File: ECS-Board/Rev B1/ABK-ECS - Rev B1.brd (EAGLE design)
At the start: 100 x 80 mm, 271 parts, among them J1 USB-B-S-RA, J10 FTSH-105-01-L-DV-NOPASTE, J11 22-05-7028-02, J12 RB1-125BAG1A, J2 MSTBA2, J3 22-05-7068-06, J4 22-05-7028-02, J5 22-05-7068-06, J6 22-05-7068-06, J7 22-05-7068-06, J8 22-05-7028-02, J9 FTSH-103-01-L-DV-NOPASTE, K1 G6K-2G-Y, SW1 B3FS-1015, SW2 B3FS-1015, T1 MMBT2907ALT3, T10 MMBT2222AL, T11 IRLML5103TRPBF, T12 MMBT2222AL, T13 IRLML5103TRPBF, T14 IRLML5103TRPBF, T15 IRLML5103TRPBF, T16 IRLML5103TRPBF, T17 MMBT2222AL, T18 MMBT2222AL, T19 MMBT2222AL, T2 EXMACHINA-LOGO-NAME, T20 MMBT2222AL, T3 IRLML5103TRPBF, T4 IRLML5103TRPBF, T5 IRLML5103TRPBF, T6 IRLML5103TRPBF, T7 MMBT2222AL, T8 MMBT2222AL, T9 MMBT2222AL, U1 AT24C512C-SSHM-B, U2 LPC1768FBD100, U3 LT3686HDDPBF, U4 LT3686HDDPBF, U5 CD4050BD, U6 CD4050BD, U7 DP83848JSQ/NOPB, X1 FC-135, X2 ASE-12, X3 3000, X4 ASE_50

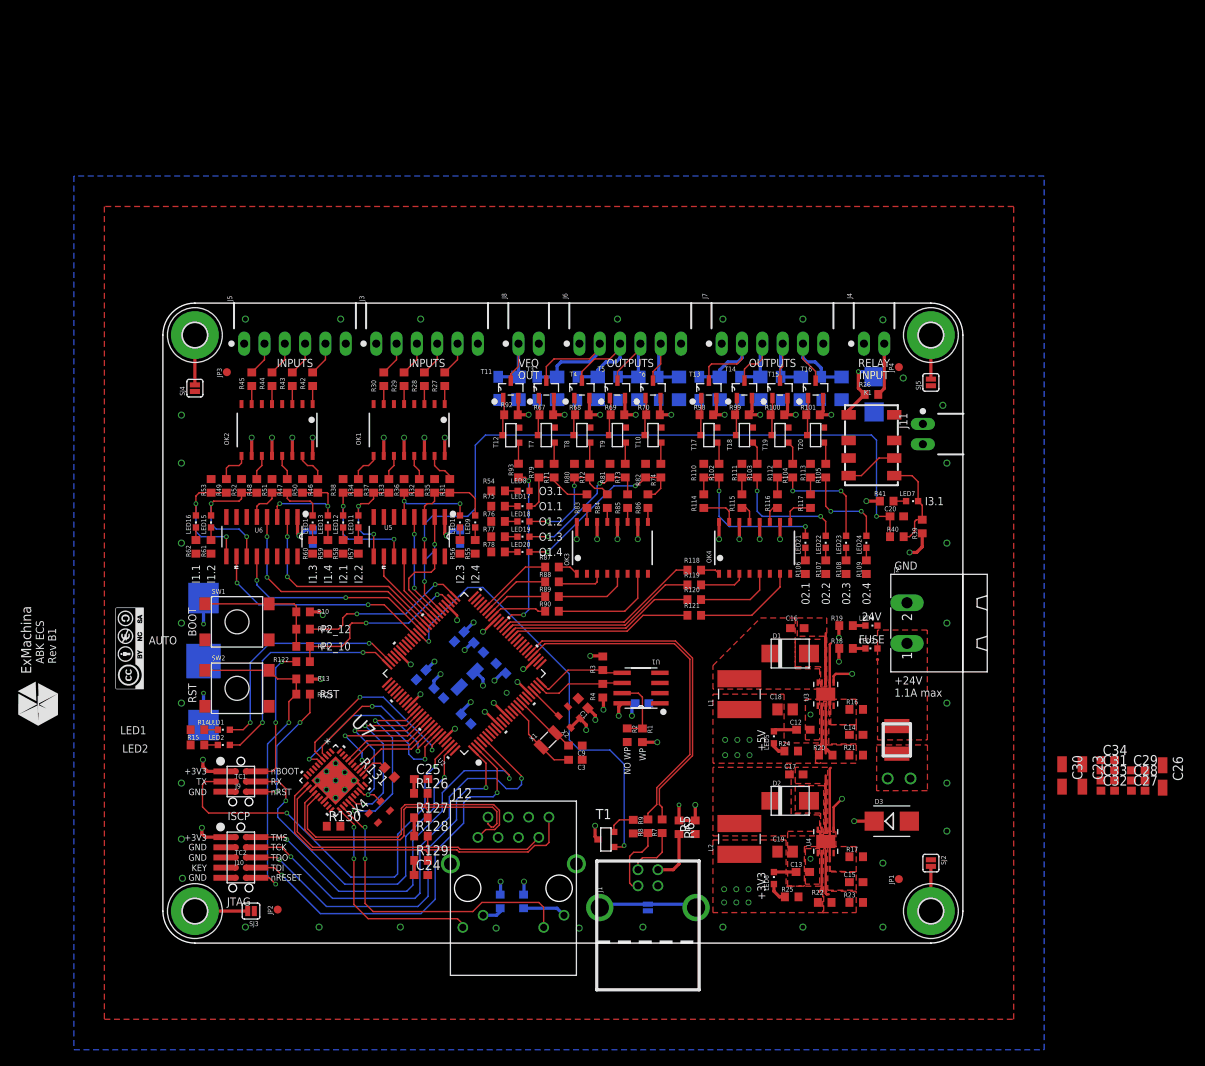
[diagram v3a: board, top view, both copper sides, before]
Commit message: Finish to route the board
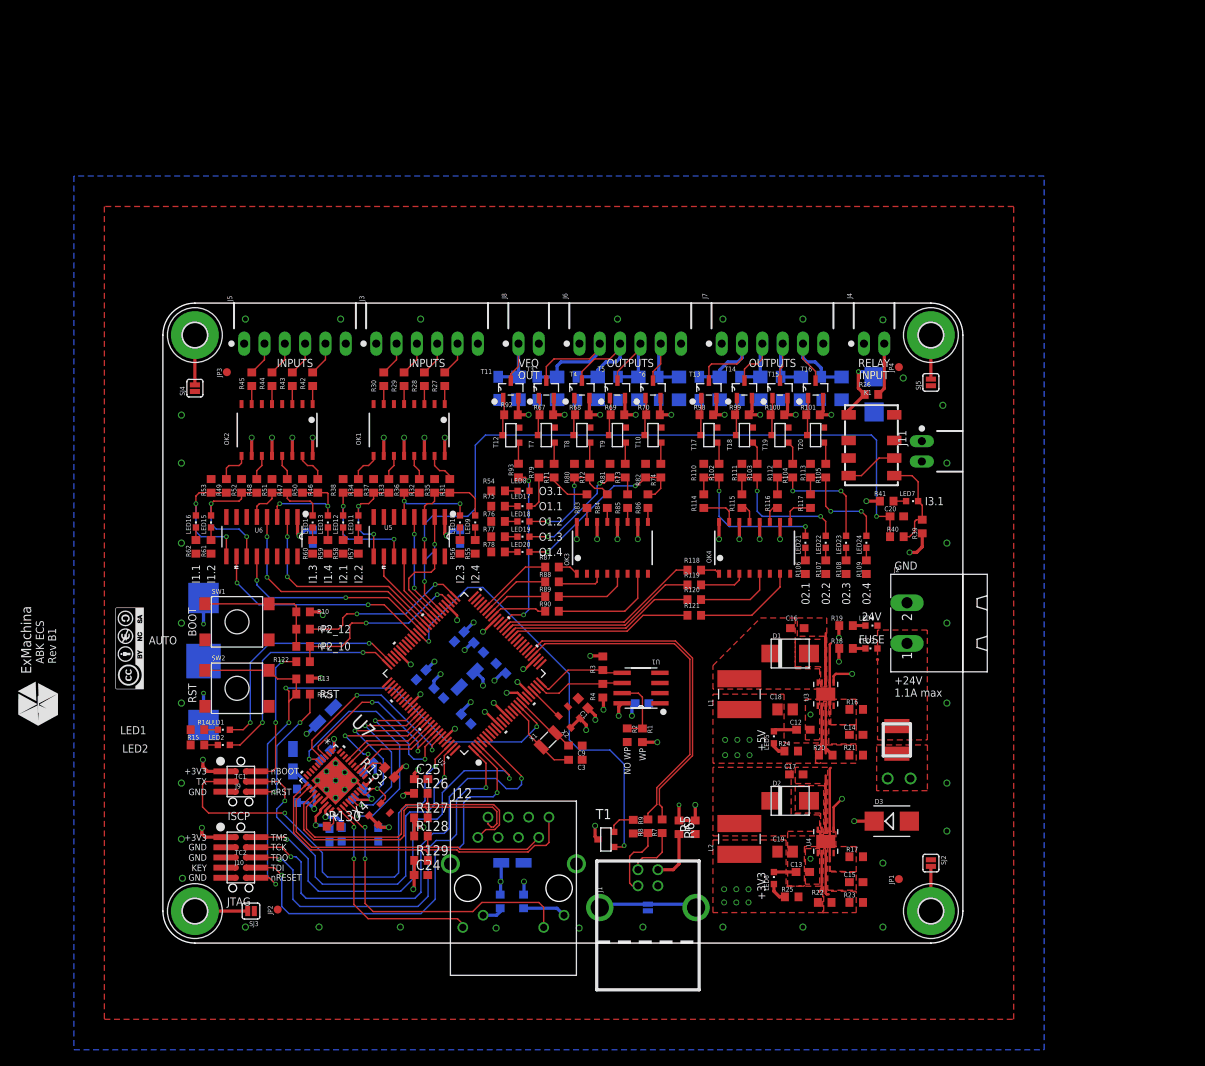
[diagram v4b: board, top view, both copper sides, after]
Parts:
- moved C26 108.7 mm to (16.3, 22.9), flipped to the bottom, turned to 90 degrees
- moved C28 105.2 mm to (16.8, 18.4), flipped to the bottom, turned to 90 degrees
- moved C27 99.7 mm to (22.4, 13.6), flipped to the bottom, turned to 270 degrees
- moved C33 97.8 mm to (20.3, 23.5), flipped to the bottom, turned to 315 degrees
- moved C32 97.4 mm to (20.8, 13.5), flipped to the bottom, turned to 270 degrees
- moved C29 96.3 mm to (25.7, 22.0), flipped to the bottom, turned to 315 degrees
- moved C31 93.8 mm to (24.4, 18.7), flipped to the bottom, turned to 315 degrees
- moved C30 92.4 mm to (20.3, 28.4), flipped to the bottom, turned to 135 degrees
- moved C34 91.7 mm to (26.9, 13.6), flipped to the bottom, turned to 270 degrees
- moved C23 72.1 mm to (43.7, 10.0), flipped to the bottom, turned to 180 degrees
- moved J11 2.16 mm to (94.9, 61.5)
- moved X4 0.25 mm to (27.1, 16.1)
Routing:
- net !RESET: track 43.5 -> 83.9 mm, vias 2 -> 4
- net PFBOUT: track 0.00 -> 28.7 mm, vias 0 -> 3
- net +3V3: track 83.1 -> 111.1 mm, vias 37 -> 47
- net AGND: track 0.00 -> 15.8 mm
- net JTAG_TDI: track 51.7 -> 55.5 mm
- net JTAG_TDO: track 49.0 -> 52.2 mm
- net JTAG_TCK: track 56.5 -> 59.7 mm
- net VBAT+: track 62.2 -> 59.1 mm
- net ISP_RXDO: track 47.7 -> 50.6 mm
- net N$116: track 0.00 -> 2.77 mm
- net JTAG_TMS: track 53.0 -> 55.6 mm
- net ISP_TXDO: track 54.1 -> 56.7 mm
- net ETH_X1: track 21.6 -> 23.7 mm
- net ETH_MDIO: track 22.7 -> 24.2 mm
- net ETH_TXD_EN: track 21.9 -> 23.1 mm
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
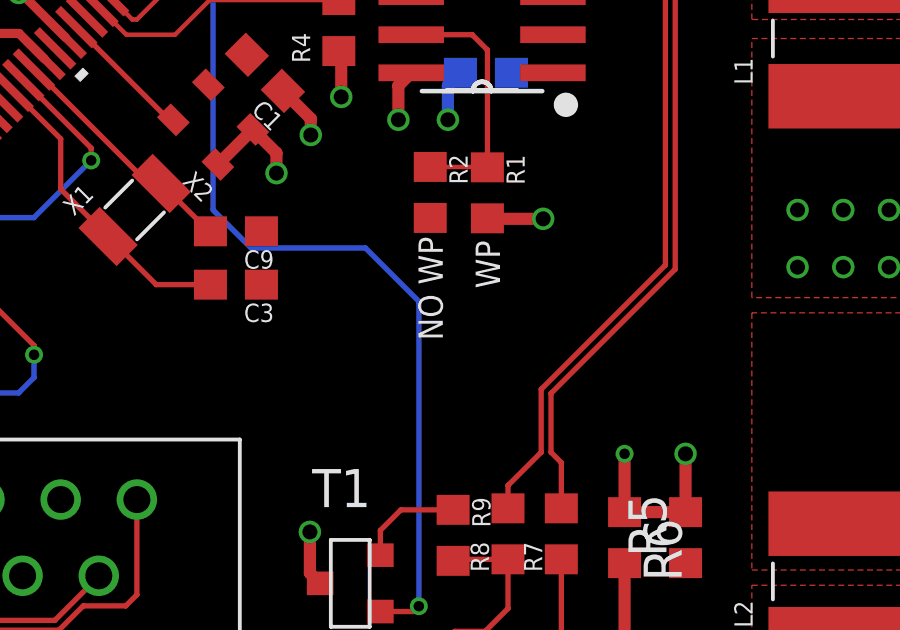
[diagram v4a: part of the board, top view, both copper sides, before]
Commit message: Add 0R to the USB Pull-up
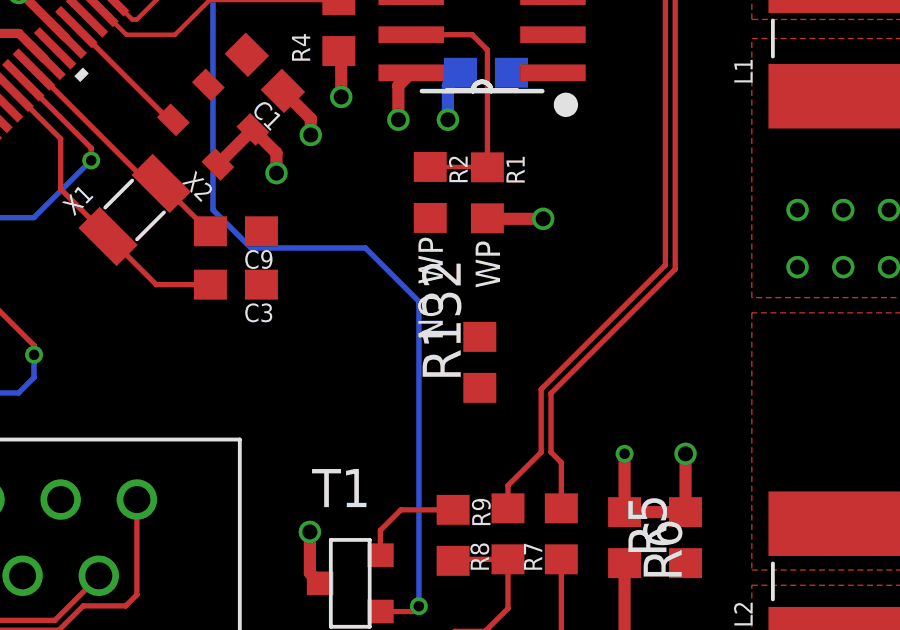
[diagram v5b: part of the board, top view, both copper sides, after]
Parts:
- added R132: 0R, rcl:R0603
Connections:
- net +3V3: now also R132.1
- net N$30: now also R132.2
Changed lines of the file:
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@@
 <layer number="14" name="Route14" color="1" fill="6" visible="no" active="no"/>
 <layer number="15" name="Route15" color="19" fill="1" visible="no" active="yes"/>
-<layer number="16" name="Bottom" color="21" fill="1" visible="no" active="yes"/>
+<layer number="16" name="Bottom" color="21" fill="1" visible="yes" active="yes"/>
 <layer number="17" name="Pads" color="18" fill="1" visible="yes" active="yes"/>
 <layer number="18" name="Vias" color="38" fill="1" visible="yes" active="yes"/>
@@
 <layer number="20" name="Dimension" color="7" fill="1" visible="yes" active="yes"/>
 <layer number="21" name="tPlace" color="55" fill="1" visible="yes" active="yes"/>
-<layer number="22" name="bPlace" color="54" fill="1" visible="no" active="yes"/>
+<layer number="22" name="bPlace" color="54" fill="1" visible="yes" active="yes"/>
 <layer number="23" name="tOrigins" color="15" fill="1" visible="yes" active="yes"/>
-<layer number="24" name="bOrigins" color="15" fill="1" visible="no" active="yes"/>
+<layer number="24" name="bOrigins" color="15" fill="1" visible="yes" active="yes"/>
 <layer number="25" name="tNames" color="55" fill="1" visible="no" active="yes"/>
-<layer number="26" name="bNames" color="54" fill="1" visible="no" active="yes"/>
+<layer number="26" name="bNames" color="54" fill="1" visible="yes" active="yes"/>
 <layer number="27" name="tValues" color="53" fill="1" visible="no" active="yes"/>
-<layer number="28" name="bValues" color="52" fill="1" visible="no" active="yes"/>
+<layer number="28" name="bValues" color="52" fill="1" visible="yes" active="yes"/>
 <layer number="29" name="tStop" color="7" fill="3" visible="no" active="yes"/>
 <layer number="30" name="bStop" color="7" fill="6" visible="no" active="yes"/>
@@
 <layer number="50" name="dxf" color="7" fill="1" visible="no" active="yes"/>
 <layer number="51" name="tDocu" color="55" fill="1" visible="yes" active="yes"/>
-<layer number="52" name="bDocu" color="54" fill="1" visible="no" active="yes"/>
+<layer number="52" name="bDocu" color="54" fill="1" visible="yes" active="yes"/>
 <layer number="53" name="tGND_GNDA" color="7" fill="1" visible="no" active="yes"/>
 <layer number="54" name="bGND_GNDA" color="7" fill="1" visible="no" active="yes"/>
@@
 <attribute name="OC_NEWARK" value="25M1728" x="284.099" y="1.778" size="1.778" layer="27" rot="R90" display="off"/>
 </element>
+<element name="R132" library="rcl" package="R0603" value="0R" x="59.69" y="20.32" rot="R90">
+<attribute name="MPN" value="RC0603FR-070RL" x="59.69" y="20.32" size="1.778" layer="27" rot="R90" display="off"/>
+<attribute name="OC_NEWARK" value="50Y7761" x="59.69" y="20.32" size="1.778" layer="27" rot="R90" display="off"/>
+<attribute name="MF" value="" x="59.69" y="20.32" size="1.778" layer="27" rot="R90" display="off"/>
+</element>
 </elements>
 <signals>
@@
 <wire x1="31.408003125" y1="8.511965625" x2="31.408003125" y2="6.8375625" width="0.4064" layer="1"/>
 <wire x1="31.408003125" y1="6.8375625" x2="31.29985" y2="6.729409375" width="0.4064" layer="1"/>
+<contactref element="R132" pad="1"/>
+<wire x1="54.026" y1="14.6685" x2="59.69" y2="19.47" width="0" layer="19" extent="1-1"/>
 </signal>
 <signal name="JTAG_TDO" class="1">
@@
 <wire x1="56.3753" y1="14.7193" x2="57.06" y2="15.404" width="0.1778" layer="1"/>
 <wire x1="57.06" y1="15.404" x2="58.801" y2="15.404" width="0.1778" layer="1"/>
+<contactref element="R132" pad="2"/>
+<wire x1="58.801" y1="15.404" x2="59.69" y2="21.17" width="0" layer="19" extent="1-1"/>
 </signal>
 <signal name="USB_CONNECT">

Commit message: Routing improvement
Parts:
- R132: value 0R -> 0R, DNI
- moved T2 40.3 mm to (16.1, 5.03), turned to 0 degrees
- moved CC1 38.0 mm to (23.6, 10.9), turned to 0 degrees
- moved R132 5.59 mm to (55.4, 16.8), turned to 0 degrees
- moved C26 0.13 mm to (16.4, 22.9)
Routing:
- net N$30: track 3.53 -> 7.10 mm
- net +3V3: track 111.1 -> 113.0 mm, vias 47 -> 48
- net ISP_RXDO: track 50.6 -> 51.2 mm
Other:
- board text added: "ISP_BOOT"
- board text added: "ISP_RST"
- board text removed: "AUTO"

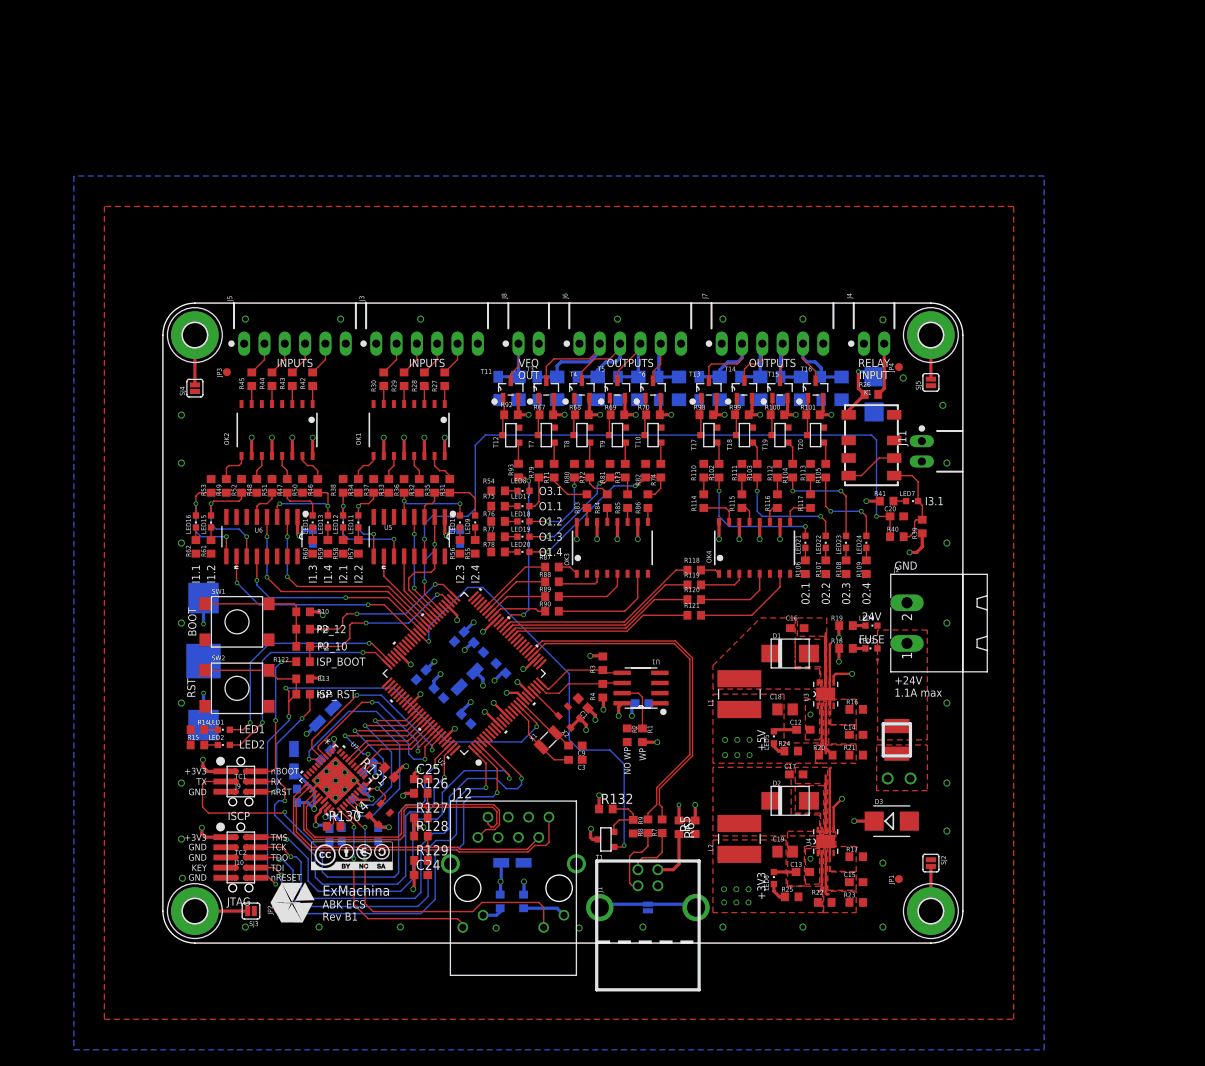
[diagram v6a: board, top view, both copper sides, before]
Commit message: Resize board 100x100mm
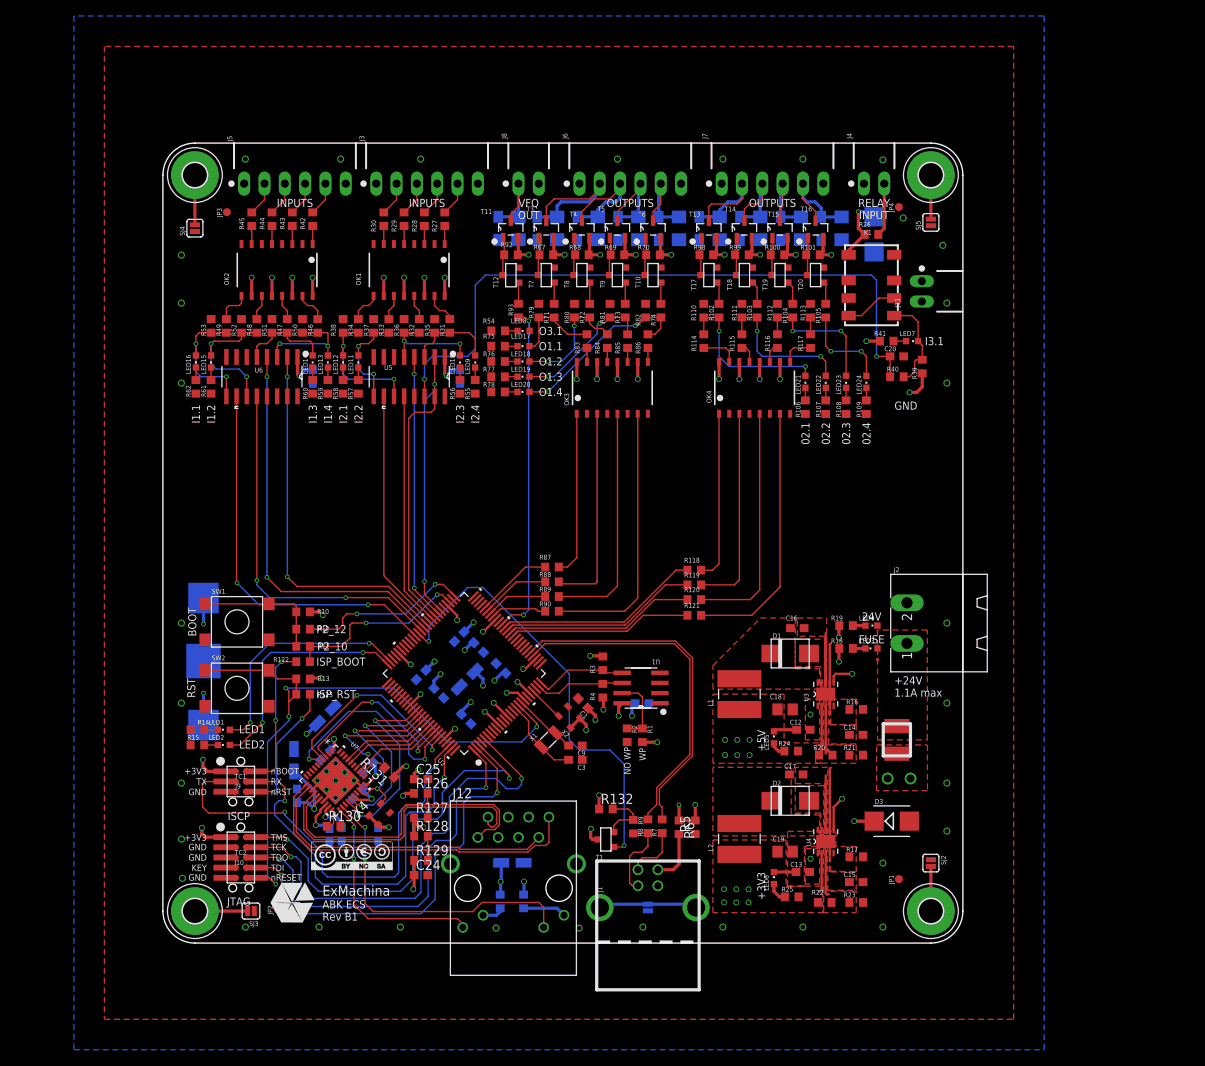
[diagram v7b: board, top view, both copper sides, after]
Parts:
- moved K1 20.0 mm to (88.6, 82.2)
- moved LED21 20.0 mm to (80.3, 70.2)
- moved LED22 20.0 mm to (82.9, 70.2)
- moved LED23 20.0 mm to (85.4, 70.2)
- moved LED24 20.0 mm to (87.9, 70.2)
- moved LED7 20.0 mm to (93.7, 75.2)
- moved OK3 20.0 mm to (56.2, 69.4)
- moved OK4 20.0 mm to (74.0, 69.4)
- moved R102 20.0 mm to (69.5, 79.1)
- moved R103 20.0 mm to (74.3, 79.1)
- moved R104 20.0 mm to (78.7, 79.1)
- moved R105 20.0 mm to (82.9, 79.1)
- moved R110 20.0 mm to (67.6, 79.1)
- moved R111 20.0 mm to (72.4, 79.1)
- moved R112 20.0 mm to (76.8, 79.1)
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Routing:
- net INPUT1.2_MCU: track 26.5 -> 46.5 mm
- net INPUT3.1_MCU: track 11.4 -> 31.4 mm
- net INPUT2.1_MCU: track 9.30 -> 29.3 mm
- net INPUT1.1_MCU: track 28.4 -> 48.4 mm
- net INPUT2.4_MCU: track 13.1 -> 33.1 mm
- net INPUT1.3_MCU: track 29.8 -> 49.8 mm
- net N$93: track 9.86 -> 29.9 mm
- net N$92: track 13.0 -> 33.0 mm
- net N$91: track 5.81 -> 25.8 mm
- net N$46: track 9.41 -> 29.4 mm
- net N$42: track 6.02 -> 26.0 mm
- net INPUT2.3_MCU: track 13.3 -> 33.3 mm
- net INPUT1.4_MCU: track 27.4 -> 47.4 mm
- net OUTPUT3.2_MCU: track 23.0 -> 43.0 mm
- net N$43: track 13.6 -> 33.6 mm
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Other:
- board size 100 x 80 mm -> 100 x 100 mm
